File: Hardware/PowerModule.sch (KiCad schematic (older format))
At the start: 25 parts, among them J1 Screw_Terminal_01x02, U2 LM2596S-5, U3 LM1117-3.3, U4 LM1117-3.3, U5 LM1117-3.3

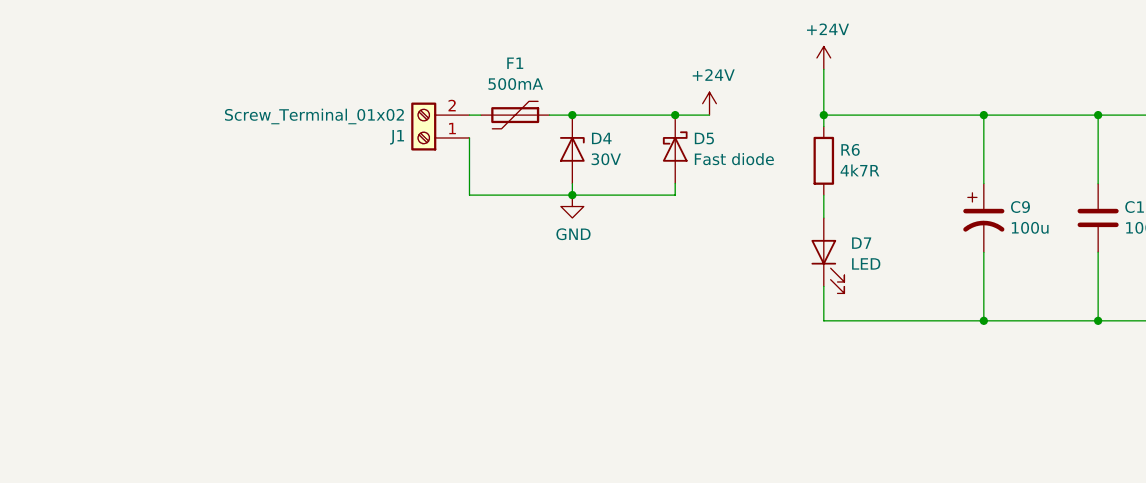
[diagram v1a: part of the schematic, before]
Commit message: Components labels placed
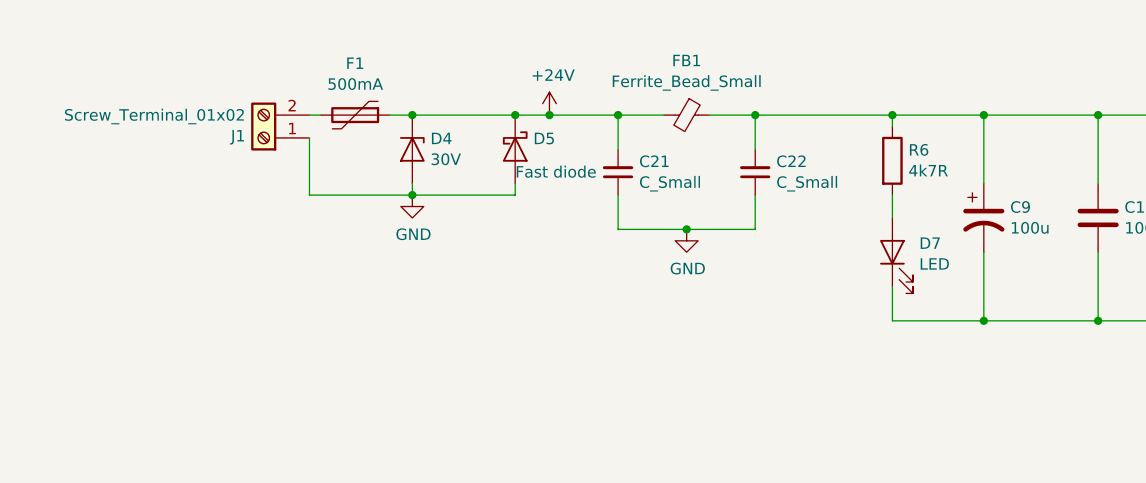
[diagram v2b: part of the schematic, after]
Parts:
- added C21, C22: C_Small, Capacitor_SMD:C_1206_3216Metric, symbol Device:C_Small
- added FB1: Ferrite_Bead_Small, Inductor_SMD:L_0805_2012Metric, symbol Device:Ferrite_Bead_Small
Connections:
- net +24V: now also C21.2, FB1.2; no longer C10.1, C9.1, R6.1, U2.1 (VIN)
- net GND: now also C21.1, C22.1
- new net: C10.1, C22.2, C9.1, FB1.1, R6.1, U2.1 (VIN)
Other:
- moved on the sheet: D4, D5, D7, F1, J1, R6
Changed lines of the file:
@@
 L Device:LED D7
 U 1 1 5F616B87
-P 3150 2550
-F 0 "D7" V 3188 2433 50  0000 R CNN
-F 1 "LED" V 3097 2433 50  0000 R CNN
-F 2 "LED_SMD:LED_0805_2012Metric" H 3150 2550 50  0001 C CNN
-F 3 "~" H 3150 2550 50  0001 C CNN
-	1    3150 2550
+P 3450 2550
+F 0 "D7" V 3488 2433 50  0000 R CNN
+F 1 "LED" V 3397 2433 50  0000 R CNN
+F 2 "LED_SMD:LED_0805_2012Metric" H 3450 2550 50  0001 C CNN
+F 3 "~" H 3450 2550 50  0001 C CNN
+	1    3450 2550
 	0    -1   -1   0
 $EndComp
@@
 L Device:R R6
 U 1 1 5F616C74
-P 3150 2150
-F 0 "R6" H 3220 2196 50  0000 L CNN
-F 1 "4k7R" H 3220 2105 50  0000 L CNN
-F 2 "Resistor_SMD:R_1206_3216Metric" V 3080 2150 50  0001 C CNN
-F 3 "~" H 3150 2150 50  0001 C CNN
-	1    3150 2150
+P 3450 2150
+F 0 "R6" H 3520 2196 50  0000 L CNN
+F 1 "4k7R" H 3520 2105 50  0000 L CNN
+F 2 "Resistor_SMD:R_1206_3216Metric" V 3380 2150 50  0001 C CNN
+F 3 "~" H 3450 2150 50  0001 C CNN
+	1    3450 2150
 	1    0    0    -1
 $EndComp
@@
 	4800 1950 4350 1950
 Wire Wire Line
-	3150 1750 3150 1950
-Wire Wire Line
-	3150 1950 3150 2000
-Connection ~ 3150 1950
-Wire Wire Line
-	3150 2300 3150 2400
-Wire Wire Line
-	3150 2700 3150 2850
-Wire Wire Line
-	3150 2850 3850 2850
+	3450 1950 3450 2000
+Wire Wire Line
+	3450 2300 3450 2400
+Wire Wire Line
+	3450 2700 3450 2850
 Wire Wire Line
 	5300 2850 5300 2900
@@
 Connection ~ 3850 1950
 Wire Wire Line
-	3850 1950 3150 1950
+	3850 1950 3450 1950
 Wire Wire Line
 	3850 2550 3850 2850
@@
 	0    1    1    0
 $EndComp
-$Comp
-L power:+24V #PWR08
-U 1 1 6075E828
-P 3150 1750
-F 0 "#PWR08" H 3150 1600 50  0001 C CNN
-F 1 "+24V" H 3165 1923 50  0000 C CNN
-F 2 "" H 3150 1750 50  0001 C CNN
-F 3 "" H 3150 1750 50  0001 C CNN
-	1    3150 1750
-	1    0    0    -1
-$EndComp
 Wire Wire Line
 	7250 1950 7250 2150
@@
 	7250 2500 7250 2550
 Wire Wire Line
-	2500 2250 2500 2300
+	1800 2250 1800 2300
 $Comp
 L power:+24V #PWR09
 U 1 1 6075E223
-P 2650 1950
-F 0 "#PWR09" H 2650 1800 50  0001 C CNN
-F 1 "+24V" H 2665 2123 50  0000 C CNN
-F 2 "" H 2650 1950 50  0001 C CNN
-F 3 "" H 2650 1950 50  0001 C CNN
-	1    2650 1950
+P 1950 1950
+F 0 "#PWR09" H 1950 1800 50  0001 C CNN
+F 1 "+24V" H 1965 2123 50  0000 C CNN
+F 2 "" H 1950 1950 50  0001 C CNN
+F 3 "" H 1950 1950 50  0001 C CNN
+	1    1950 1950
 	1    0    0    -1
 $EndComp
@@
 L power:GND #PWR011
 U 1 1 5F8FD0C8
-P 2050 2300
-F 0 "#PWR011" H 2050 2050 50  0001 C CNN
-F 1 "GND" H 2055 2127 50  0000 C CNN
-F 2 "" H 2050 2300 50  0001 C CNN
-F 3 "" H 2050 2300 50  0001 C CNN
-	1    2050 2300
-	1    0    0    -1
-$EndComp
-Wire Wire Line
-	1600 2300 2050 2300
-Wire Wire Line
-	2050 2300 2500 2300
-Connection ~ 2050 2300
-Wire Wire Line
-	1600 2300 1600 2050
-Wire Wire Line
-	1600 1950 1650 1950
-Wire Wire Line
-	2050 2300 2050 2250
-Wire Wire Line
-	1950 1950 2050 1950
-Connection ~ 2050 1950
+P 1350 2300
+F 0 "#PWR011" H 1350 2050 50  0001 C CNN
+F 1 "GND" H 1355 2127 50  0000 C CNN
+F 2 "" H 1350 2300 50  0001 C CNN
+F 3 "" H 1350 2300 50  0001 C CNN
+	1    1350 2300
+	1    0    0    -1
+$EndComp
+Wire Wire Line
+	900  2300 1350 2300
+Wire Wire Line
+	1350 2300 1800 2300
+Connection ~ 1350 2300
+Wire Wire Line
+	900  2300 900  2050
+Wire Wire Line
+	900  1950 950  1950
+Wire Wire Line
+	1350 2300 1350 2250
+Wire Wire Line
+	1250 1950 1350 1950
+Connection ~ 1350 1950
 $Comp
 L Device:D_Zener D?
 U 1 1 5F8E1DF0
-P 2050 2100
+P 1350 2100
 AR Path="/5F8E1DF0" Ref="D?"  Part="1"
 AR Path="/5F60F829/5F8E1DF0" Ref="D4"  Part="1"
-F 0 "D4" V 2004 2179 50  0000 L CNN
-F 1 "30V" V 2095 2179 50  0000 L CNN
-F 2 "Diode_SMD:D_SMB" H 2050 2100 50  0001 C CNN
-F 3 "~" H 2050 2100 50  0001 C CNN
-	1    2050 2100
+F 0 "D4" V 1304 2179 50  0000 L CNN
+F 1 "30V" V 1395 2179 50  0000 L CNN
+F 2 "Diode_SMD:D_SMB" H 1350 2100 50  0001 C CNN
+F 3 "~" H 1350 2100 50  0001 C CNN
+	1    1350 2100
 	0    1    1    0
 $EndComp
@@
 L Device:Polyfuse F?
 U 1 1 5F8E1DE4
-P 1800 1950
+P 1100 1950
 AR Path="/5F8E1DE4" Ref="F?"  Part="1"
 AR Path="/5F60F829/5F8E1DE4" Ref="F1"  Part="1"
-F 0 "F1" V 1575 1950 50  0000 C CNN
-F 1 "500mA" V 1666 1950 50  0000 C CNN
-F 2 "Fuse:Fuse_2010_5025Metric" H 1850 1750 50  0001 L CNN
-F 3 "~" H 1800 1950 50  0001 C CNN
-	1    1800 1950
+F 0 "F1" V 875 1950 50  0000 C CNN
+F 1 "500mA" V 966 1950 50  0000 C CNN
+F 2 "Fuse:Fuse_2010_5025Metric" H 1150 1750 50  0001 L CNN
+F 3 "~" H 1100 1950 50  0001 C CNN
+	1    1100 1950
 	0    1    1    0
 $EndComp
@@
 L Connector:Screw_Terminal_01x02 J?
 U 1 1 5F8E1DD8
-P 1400 2050
+P 700 2050
 AR Path="/5F8E1DD8" Ref="J?"  Part="1"
 AR Path="/5F60F829/5F8E1DD8" Ref="J1"  Part="1"
-F 0 "J1" H 1480 2042 50  0000 L CNN
-F 1 "Screw_Terminal_01x02" H 1480 1951 50  0000 L CNN
-F 2 "TerminalBlock:TerminalBlock_bornier-2_P5.08mm" H 1400 2050 50  0001 C CNN
-F 3 "~" H 1400 2050 50  0001 C CNN
-	1    1400 2050
+F 0 "J1" H 780 2042 50  0000 L CNN
+F 1 "Screw_Terminal_01x02" H 780 1951 50  0000 L CNN
+F 2 "TerminalBlock:TerminalBlock_bornier-2_P5.08mm" H 700 2050 50  0001 C CNN
+F 3 "~" H 700 2050 50  0001 C CNN
+	1    700  2050
 	-1   0    0    1
 $EndComp
 Wire Wire Line
-	2050 1950 2500 1950
-Wire Wire Line
-	2500 1950 2650 1950
-Connection ~ 2500 1950
+	1350 1950 1800 1950
+Wire Wire Line
+	1800 1950 1950 1950
+Connection ~ 1800 1950
 $Comp
 L Device:D_Schottky D5
 U 1 1 5F8F78E9
-P 2500 2100
-F 0 "D5" V 2454 2179 50  0000 L CNN
-F 1 "Fast diode" V 2545 2179 50  0000 L CNN
-F 2 "Diode_SMD:D_SMB" H 2500 2100 50  0001 C CNN
-F 3 "~" H 2500 2100 50  0001 C CNN
-	1    2500 2100
+P 1800 2100
+F 0 "D5" V 1754 2179 50  0000 L CNN
+F 1 "Fast diode" V 1900 2100 50  0000 L CNN
+F 2 "Diode_SMD:D_SMB" H 1800 2100 50  0001 C CNN
+F 3 "~" H 1800 2100 50  0001 C CNN
+	1    1800 2100
 	0    1    1    0
 $EndComp
@@
 Wire Wire Line
 	6200 5800 6250 5800
+Wire Wire Line
+	3450 2850 3850 2850
+Connection ~ 3450 1950
+$Comp
+L Device:C_Small C21
+U 1 1 60AE0932
+P 2250 2200
+F 0 "C21" H 2158 2154 50  0000 R CNN
+F 1 "C_Small" H 2158 2245 50  0000 R CNN
+F 2 "Capacitor_SMD:C_1206_3216Metric" H 2250 2200 50  0001 C CNN
+F 3 "~" H 2250 2200 50  0001 C CNN
+	1    2250 2200
+	-1   0    0    1
+$EndComp
+$Comp
+L Device:Ferrite_Bead_Small FB1
+U 1 1 60AE1205
+P 2550 1950
+F 0 "FB1" V 2313 1950 50  0000 C CNN
+F 1 "Ferrite_Bead_Small" V 2404 1950 50  0000 C CNN
+F 2 "Inductor_SMD:L_0805_2012Metric" V 2480 1950 50  0001 C CNN
+F 3 "~" H 2550 1950 50  0001 C CNN
+	1    2550 1950
+	0    1    1    0
+$EndComp
+$Comp
+L Device:C_Small C22
+U 1 1 60AE1BAC
+P 2850 2200
+F 0 "C22" H 2758 2154 50  0000 R CNN
+F 1 "C_Small" H 2758 2245 50  0000 R CNN
+F 2 "Capacitor_SMD:C_1206_3216Metric" H 2850 2200 50  0001 C CNN
+F 3 "~" H 2850 2200 50  0001 C CNN
+	1    2850 2200
+	-1   0    0    1
+$EndComp
+$Comp
+L power:GND #PWR0104
+U 1 1 60AE6D3C
+P 2550 2450
+F 0 "#PWR0104" H 2550 2200 50  0001 C CNN
+F 1 "GND" H 2555 2277 50  0000 C CNN
+F 2 "" H 2550 2450 50  0001 C CNN
+F 3 "" H 2550 2450 50  0001 C CNN
+	1    2550 2450
+	1    0    0    -1
+$EndComp
+Wire Wire Line
+	2250 2450 2550 2450
+Connection ~ 2550 2450
+Wire Wire Line
+	2550 2450 2850 2450
+Connection ~ 1950 1950
+Wire Wire Line
+	2850 2300 2850 2450
+Wire Wire Line
+	2250 2300 2250 2450
+Wire Wire Line
+	2650 1950 2850 1950
+Wire Wire Line
+	1950 1950 2250 1950
+Wire Wire Line
+	2250 2100 2250 1950
+Connection ~ 2250 1950
+Wire Wire Line
+	2250 1950 2450 1950
+Wire Wire Line
+	2850 2100 2850 1950
+Connection ~ 2850 1950
+Wire Wire Line
+	2850 1950 3450 1950
 $EndSCHEMATC
